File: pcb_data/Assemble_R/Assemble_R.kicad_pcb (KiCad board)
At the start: 2 copper layers, 186.9 x 96.4 mm, 103 parts, among them J1 Conn_01x02, U1 XIAO-nRF52840

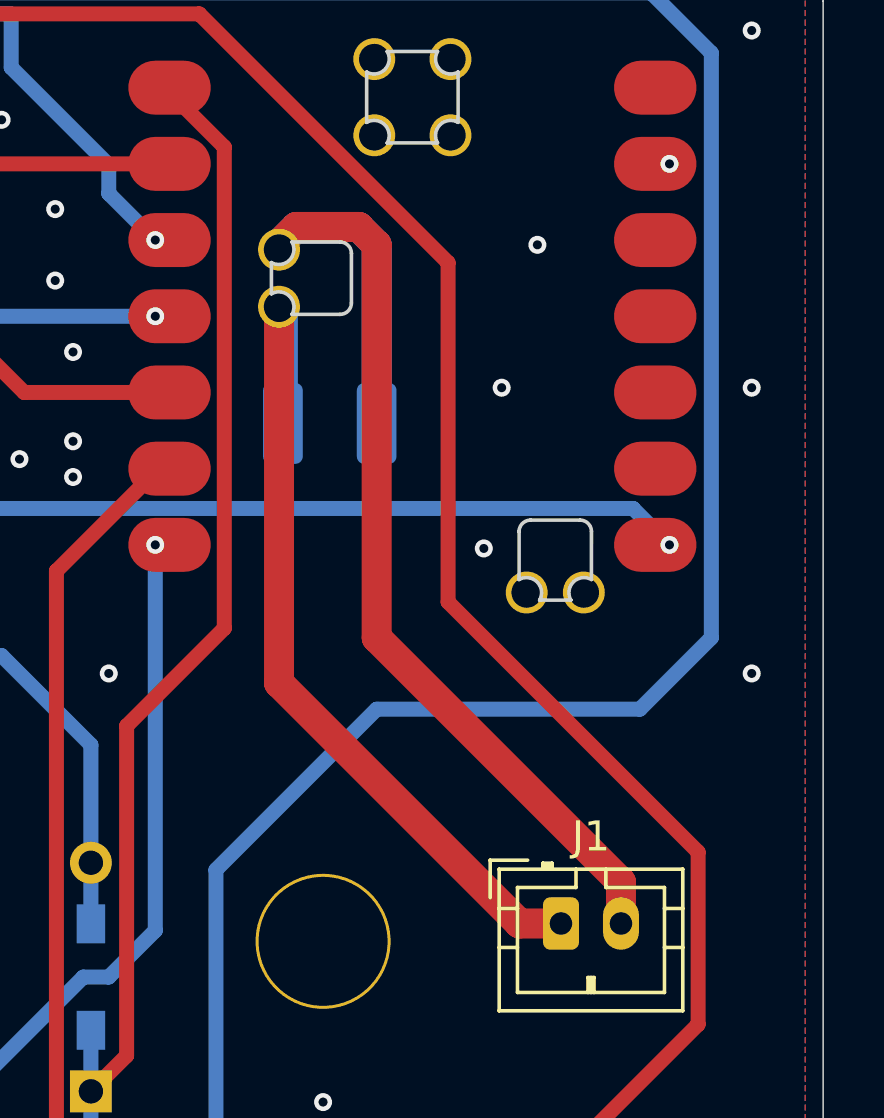
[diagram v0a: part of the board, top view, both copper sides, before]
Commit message: Feat/fix power line width (#24)
* fix power line pattern width

* project file updated
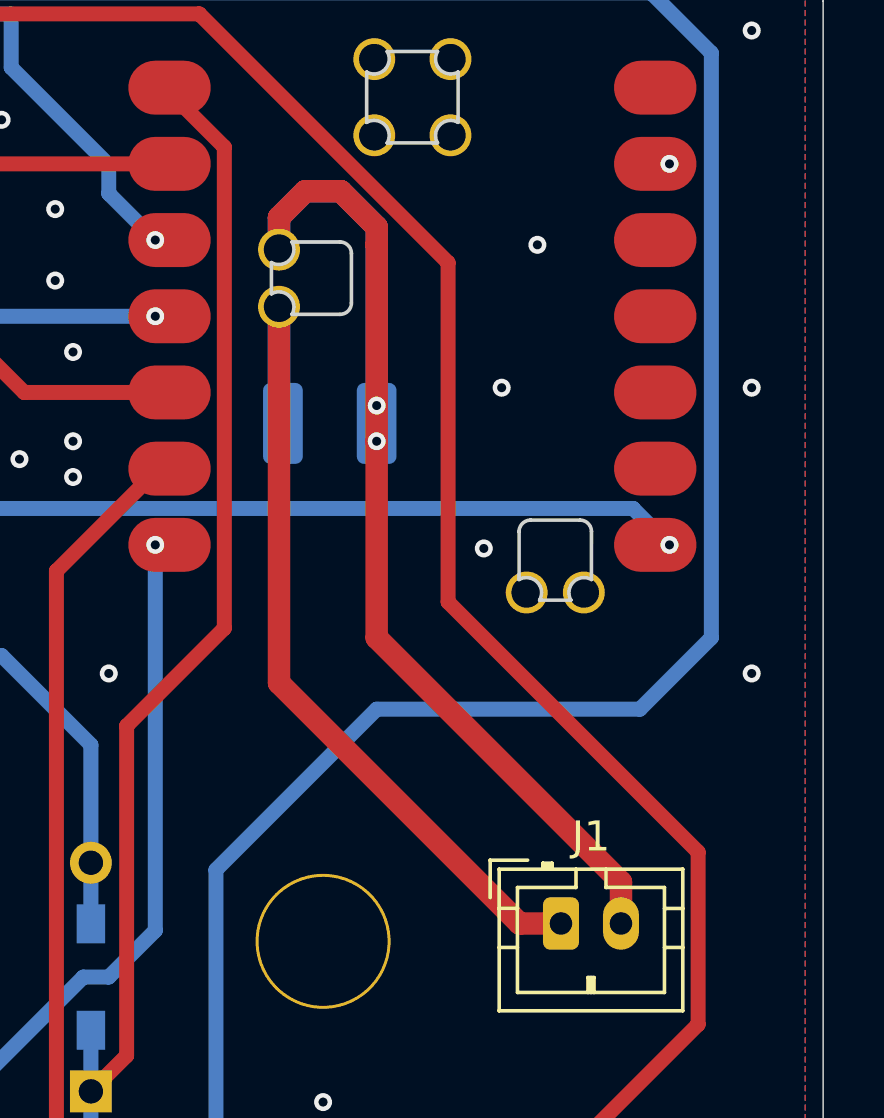
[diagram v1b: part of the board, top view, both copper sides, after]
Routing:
- net GND: track 39.8 -> 43.5 mm, vias 228 -> 230
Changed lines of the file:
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@@
+	)
+	(segment
+		(start 236.339261 55.364109)
+		(end 237.529887 56.554735)
+		(width 0.75)
+		(layer "F.Cu")
+		(net 52)
+	)
+	(segment
+		(start 235.148635 55.364109)
+		(end 236.339261 55.364109)
+		(width 0.75)
+		(layer "F.Cu")
+		(net 52)
+	)
+	(segment
+		(start 237.529887 63.698491)
+		(end 237.529887 57.150048)
+		(width 0.75)
+		(layer "F.Cu")
+		(net 52)
 	)
 	(segment
 		(start 237.529887 70.246934)
 		(end 245.673643 78.39069)
-		(width 1)
+		(width 0.75)
 		(layer "F.Cu")
 		(net 52)
@@
 	(segment
 		(start 237.529887 70.246934)
+		(end 237.529887 63.698491)
+		(width 0.75)
+		(layer "F.Cu")
+		(net 52)
+	)
+	(segment
+		(start 234.275513 56.237231)
+		(end 235.148635 55.364109)
+		(width 0.75)
+		(layer "F.Cu")
+		(net 52)
+	)
+	(segment
+		(start 237.529887 56.554735)
 		(end 237.529887 57.150048)
-		(width 1)
-		(layer "F.Cu")
-		(net 52)
-	)
-	(segment
-		(start 236.934574 56.554735)
-		(end 234.85281 56.554735)
-		(width 1)
-		(layer "F.Cu")
-		(net 52)
-	)
-	(segment
-		(start 234.85281 56.554735)
-		(end 234.275513 57.132032)
-		(width 1)
-		(layer "F.Cu")
-		(net 52)
-	)
-	(segment
-		(start 237.529887 57.150048)
-		(end 236.934574 56.554735)
-		(width 1)
+		(width 0.75)
 		(layer "F.Cu")
 		(net 52)
@@
 		(start 245.673643 78.39069)
 		(end 245.673643 79.771942)
-		(width 1)
-		(layer "F.Cu")
-		(net 52)
-	)
-	(segment
-		(start 234.275513 57.132032)
-		(end 234.275513 57.3092)
-		(width 0.5)
+		(width 0.75)
+		(layer "F.Cu")
+		(net 52)
+	)
+	(segment
+		(start 234.275513 57.3092)
+		(end 234.275513 56.237231)
+		(width 0.75)
 		(layer "F.Cu")
 		(net 52)
@@
 	)
 	(via
+		(at 237.529887 62.507865)
+		(size 0.6)
+		(drill 0.3)
+		(layers "F.Cu" "B.Cu")
+		(net 52)
+	)
+	(via
 		(at 176.2125 61.9125)
 		(size 0.6)
@@
 	)
 	(via
+		(at 237.529887 63.698491)
+		(size 0.6)
+		(drill 0.3)
+		(layers "F.Cu" "B.Cu")
+		(net 52)
+	)
+	(via
 		(at 157.162632 117.871974)
 		(size 0.6)
@@
 	)
 	(segment
-		(start 237.529887 57.150048)
+		(start 236.339261 55.364109)
+		(end 237.529887 56.554735)
+		(width 0.75)
+		(layer "B.Cu")
+		(net 52)
+	)
+	(segment
+		(start 237.529887 56.554735)
+		(end 237.529887 62.507865)
+		(width 0.75)
+		(layer "B.Cu")
+		(net 52)
+	)
+	(segment
+		(start 237.529887 62.507865)
 		(end 237.529887 63.103178)
-		(width 1)
-		(layer "B.Cu")
-		(net 52)
-	)
-	(segment
-		(start 234.85281 56.554735)
-		(end 236.934574 56.554735)
-		(width 1)
-		(layer "B.Cu")
-		(net 52)
-	)
-	(segment
-		(start 236.934574 56.554735)
-		(end 237.529887 57.150048)
-		(width 1)
-		(layer "B.Cu")
-		(net 52)
-	)
-	(segment
-		(start 234.275513 57.132032)
-		(end 234.85281 56.554735)
-		(width 1)
+		(width 0.75)
+		(layer "B.Cu")
+		(net 52)
+	)
+	(segment
+		(start 235.148635 55.364109)
+		(end 236.339261 55.364109)
+		(width 0.75)
 		(layer "B.Cu")
 		(net 52)
@@
 	(segment
 		(start 234.275513 57.3092)
-		(end 234.275513 57.132032)
-		(width 0.5)
+		(end 234.275513 56.237231)
+		(width 0.75)
+		(layer "B.Cu")
+		(net 52)
+	)
+	(segment
+		(start 234.275513 56.237231)
+		(end 235.148635 55.364109)
+		(width 0.75)
 		(layer "B.Cu")
 		(net 52)
@@
 		(start 242.292391 79.771942)
 		(end 243.673643 79.771942)
-		(width 1)
+		(width 0.75)
 		(layer "F.Cu")
 		(net 56)
@@
 		(start 234.275513 71.755064)
 		(end 242.292391 79.771942)
-		(width 1)
+		(width 0.75)
 		(layer "F.Cu")
 		(net 56)
@@
 		(start 234.275513 59.2142)
 		(end 234.275513 71.755064)
-		(width 1)
+		(width 0.75)
 		(layer "F.Cu")
 		(net 56)
 	)
 	(segment
-		(start 234.404887 63.103178)
-		(end 234.404887 59.343574)
-		(width 1)
+		(start 234.275513 62.973804)
+		(end 234.404887 63.103178)
+		(width 0.5)
 		(layer "B.Cu")
 		(net 56)
@@
 		(layer "B.Cu")
 		(net 56)
+	)
+	(segment
+		(start 234.275513 59.2142)
+		(end 234.275513 62.973804)
+		(width 0.75)
+		(layer "B.Cu")
+		(net 56)

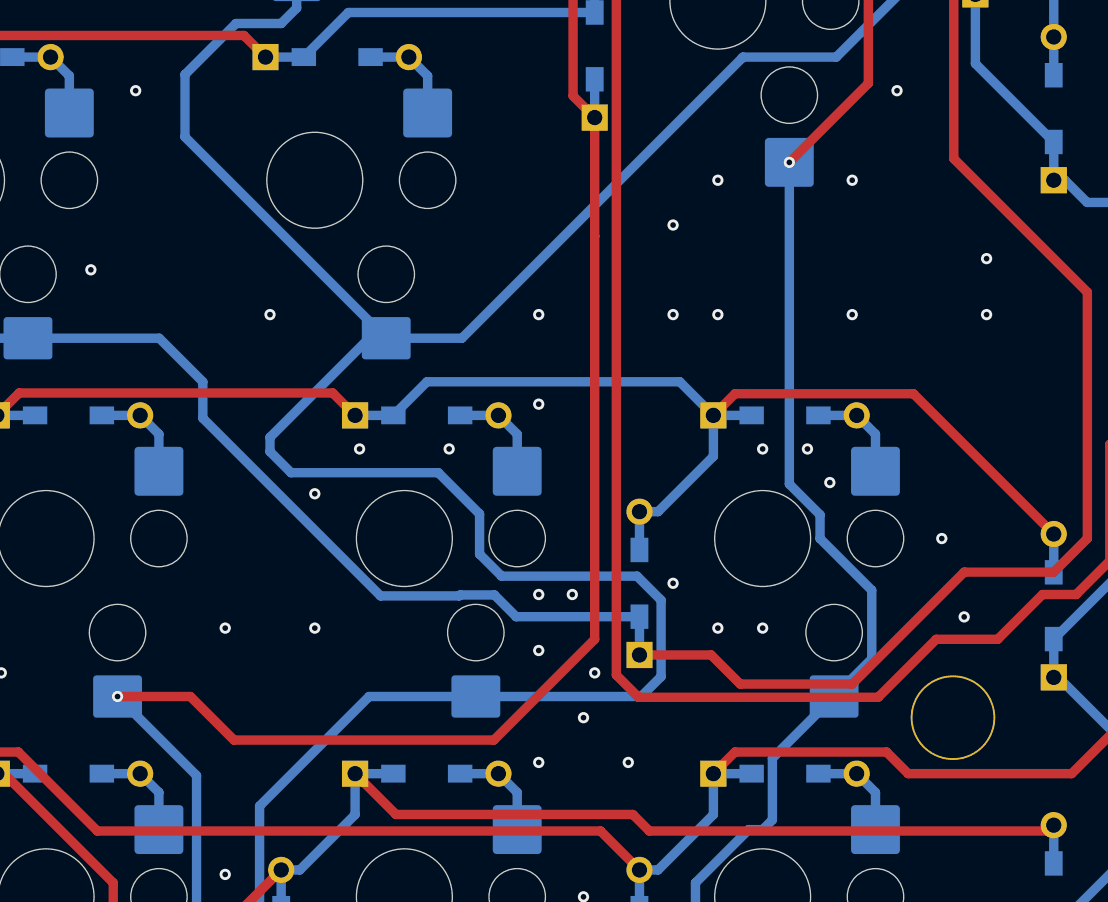
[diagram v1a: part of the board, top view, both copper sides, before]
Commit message: Issue/15 top and bottom plate (#26)
* copy from Assemble

* remove file

* rename file

* remove file

* replace value

* fix position of mounting hole

* copy from Assemble_L

* remove segment and via

* remove zone

* remove diode

* replace switch footprint

* update line

* update footprint

* remove unnecessary footprint

* add step file

* change hole position

* step updated

* add bottom_l project file

* remove unnecessary footprint

* add step file

* copy from Assemble_R

* remove zone, segment and via

* remove diode

* replace switch footprint

* update line

* remove unnecessary footprint

* add step file

* add bottom_r project file

* remove unnecessary footprint

* add step file

* fix hole footprint and number (#25)

* fix line

* Issue/12 build guide (#28)

* add build guide

* update build guide

* Update docs/requirements/requirements_board.md

* Update docs/requirements/requirements_board.md

* Update docs/requirements/requirements_board.md

* Update docs/requirements/requirements_board.md

* Update docs/requirements/requirements_board.md

* Update docs/build_guide.md

* Update docs/build_guide.md

* Update README.md

* Update docs/build_guide.md

* Update docs/build_guide.md

* Update README.md

* Update docs/build_guide.md

* Update docs/build_guide.md

* Update docs/build_guide.md

* Update docs/build_guide.md

* Update docs/build_guide.md

* Update docs/build_guide.md

* Update docs/build_guide.md

* Update docs/build_guide.md

* Update docs/build_guide.md

* Update docs/build_guide.md

* Update docs/build_guide.md

* Update docs/build_guide.md

* Update docs/build_guide.md

* Update docs/build_guide.md

* Update docs/build_guide.md

* Update docs/build_guide.md

* Update docs/build_guide.md

* Update docs/build_guide.md

* Update docs/build_guide.md

* Update docs/build_guide.md

* Update docs/build_guide.md

* Update docs/build_guide.md

* Update docs/build_guide.md

* Update docs/build_guide.md

* Update docs/build_guide.md

* Update doc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
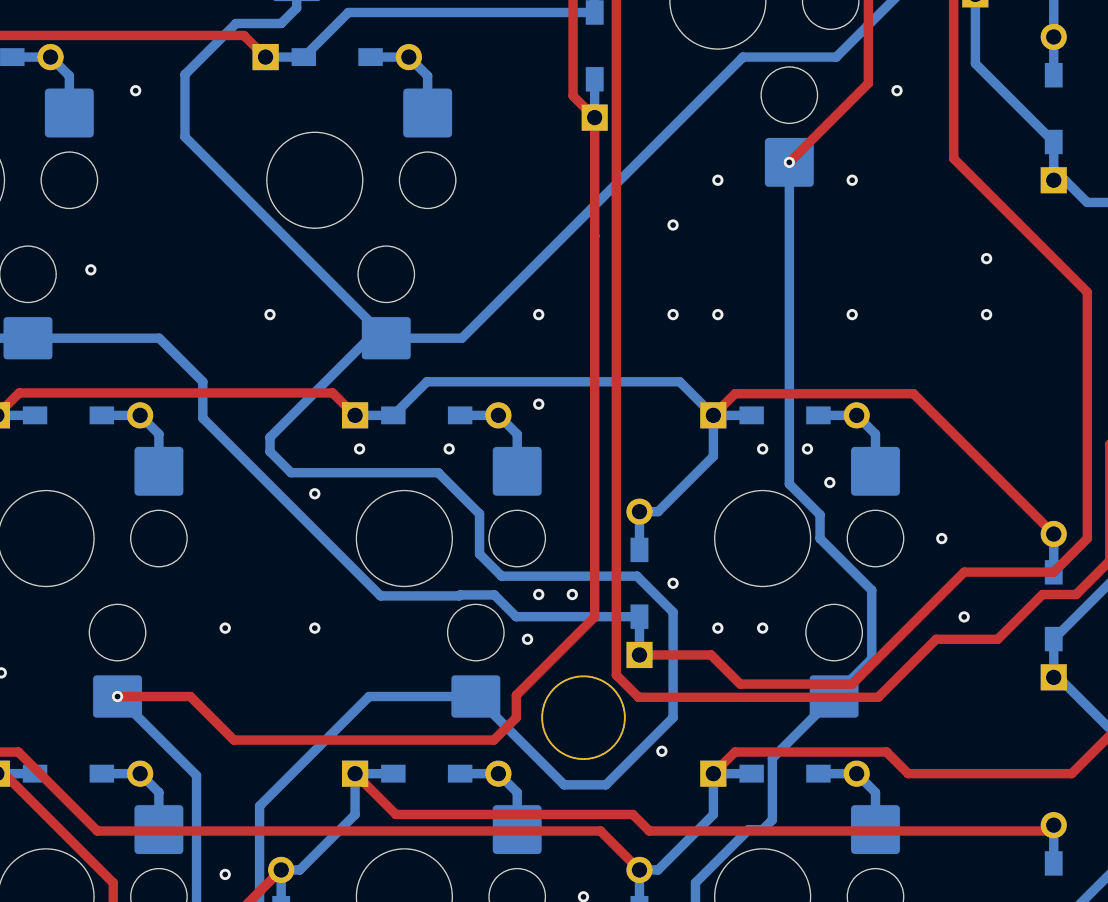
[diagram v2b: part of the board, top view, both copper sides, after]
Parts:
- moved H6 19.6 mm to (207.2, 123.8)
- renumbered H8 to H7, H7 to H8
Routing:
- net IO 12: track 232.4 -> 238.5 mm
- net GND: vias 230 -> 227
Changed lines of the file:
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@@
 	(footprint "kbd_Hole:m2_Spacer_Hole"
 		(layer "F.Cu")
-		(at 226.814253 123.825104)
+		(at 207.168924 123.825104)
 		(descr "Mounting Hole 2.2mm, no annular, M2")
 		(tags "mounting hole 2.2mm no annular m2")
@@
 		(descr "Mounting Hole 2.2mm, no annular, M2")
 		(tags "mounting hole 2.2mm no annular m2")
-		(property "Reference" "H7"
+		(property "Reference" "H8"
 			(at 0 -3.2 0)
 			(layer "F.Fab")
@@
 		(descr "Mounting Hole 2.2mm, no annular, M2")
 		(tags "mounting hole 2.2mm no annular m2")
-		(property "Reference" "H8"
+		(property "Reference" "H7"
 			(at 0 -3.2 0)
 			(layer "F.Fab")
@@
 	)
 	(segment
-		(start 207.764237 98.226719)
-		(end 207.764237 119.657913)
-		(width 0.5)
-		(layer "F.Cu")
-		(net 48)
-	)
-	(segment
-		(start 207.7642 91.9163)
-		(end 207.7642 98.226682)
-		(width 0.5)
-		(layer "F.Cu")
-		(net 48)
-	)
-	(segment
 		(start 220.26581 59.5313)
 		(end 206.6147 73.18241)
@@
 	)
 	(segment
-		(start 182.3938 141.75)
-		(end 139.5313 141.75)
+		(start 188.583177 125.01573)
+		(end 202.40642 125.01573)
 		(width 0.5)
 		(layer "F.Cu")
@@
 	)
 	(segment
-		(start 207.764237 119.657913)
-		(end 202.40642 125.01573)
+		(start 182.3938 141.75)
+		(end 139.5313 141.75)
 		(width 0.5)
 		(layer "F.Cu")
@@
 	)
 	(segment
+		(start 207.764237 118.467287)
+		(end 207.764237 98.226719)
+		(width 0.5)
+		(layer "F.Cu")
+		(net 48)
+	)
+	(segment
+		(start 207.764237 98.226719)
+		(end 207.7642 98.226682)
+		(width 0.5)
+		(layer "F.Cu")
+		(net 48)
+	)
+	(segment
 		(start 225.782275 62.0712)
 		(end 223.242375 59.5313)
@@
 	)
 	(segment
-		(start 202.40642 125.01573)
+		(start 186.267447 122.7)
 		(end 188.583177 125.01573)
 		(width 0.5)
@@
 	)
 	(segment
-		(start 188.583177 125.01573)
+		(start 182.3938 122.7)
 		(end 186.267447 122.7)
 		(width 0.5)
@@
 	)
 	(segment
-		(start 186.267447 122.7)
-		(end 182.3938 122.7)
+		(start 202.40642 125.01573)
+		(end 203.597046 123.825104)
+		(width 0.5)
+		(layer "F.Cu")
+		(net 48)
+	)
+	(segment
+		(start 203.597046 122.634478)
+		(end 207.764237 118.467287)
 		(width 0.5)
 		(layer "F.Cu")
@@
 	(segment
 		(start 207.7642 98.226682)
-		(end 207.764237 98.226719)
+		(end 207.7642 91.9163)
+		(width 0.5)
+		(layer "F.Cu")
+		(net 48)
+	)
+	(segment
+		(start 203.597046 123.825104)
+		(end 203.597046 122.634478)
 		(width 0.5)
 		(layer "F.Cu")
@@
 	)
 	(segment
-		(start 191.622065 110.801)
-		(end 199.45093 110.801)
-		(width 0.5)
-		(layer "B.Cu")
-		(net 50)
-	)
-	(segment
 		(start 196.6813 103.65)
 		(end 185.9803 92.949)
@@
 	)
 	(segment
-		(start 201.6428 115.128841)
-		(end 202.814959 116.301)
-		(width 0.5)
-		(layer "B.Cu")
-		(net 50)
-	)
-	(segment
 		(start 200.702266 103.65)
 		(end 196.6813 103.65)
@@
 	)
 	(segment
-		(start 190.50016 109.679095)
-		(end 191.622065 110.801)
-		(width 0.5)
-		(layer "B.Cu")
-		(net 50)
-	)
-	(segment
 		(start 228.600192 81.557881)
 		(end 227.752879 81.557881)
@@
 	)
 	(segment
+		(start 206.140782 127.396982)
+		(end 201.4438 122.7)
+		(width 0.5)
+		(layer "B.Cu")
+		(net 50)
+	)
+	(segment
+		(start 211.931428 118.215228)
+		(end 211.931428 123.825104)
+		(width 0.5)
+		(layer "B.Cu")
+		(net 50)
+	)
+	(segment
 		(start 215.576968 88.775299)
 		(end 200.702266 103.65)
@@
 	)
 	(segment
-		(start 190.50016 108.920905)
-		(end 190.50016 109.679095)
+		(start 201.6428 112.99287)
+		(end 201.6428 115.128841)
 		(width 0.5)
 		(layer "B.Cu")
@@
 	)
 	(segment
+		(start 196.6813 103.65)
+		(end 195.771065 103.65)
+		(width 0.5)
+		(layer "B.Cu")
+		(net 50)
+	)
+	(segment
 		(start 191.9188 84.6)
 		(end 191.9188 86.092371)
@@
 	)
 	(segment
-		(start 210.2358 122.7)
-		(end 201.4438 122.7)
-		(width 0.5)
-		(layer "B.Cu")
-		(net 50)
-	)
-	(segment
-		(start 211.295 121.6408)
-		(end 210.2358 122.7)
+		(start 201.6428 115.128841)
+		(end 202.814959 116.301)
 		(width 0.5)
 		(layer "B.Cu")
@@
 	)
 	(segment
-		(start 196.6813 103.65)
-		(end 195.771065 103.65)
+		(start 211.931428 123.825104)
+		(end 208.35955 127.396982)
 		(width 0.5)
 		(layer "B.Cu")
@@
 	)
 	(segment
+		(start 191.622065 110.801)
+		(end 199.45093 110.801)
+		(width 0.5)
+		(layer "B.Cu")
+		(net 50)
+	)
+	(segment
+		(start 202.814959 116.301)
+		(end 210.0172 116.301)
+		(width 0.5)
+		(layer "B.Cu")
+		(net 50)
+	)
+	(segment
 		(start 201.4438 122.7)
 		(end 195.771065 122.7)
@@
 	)
 	(segment
-		(start 201.6428 112.99287)
-		(end 201.6428 115.128841)
+		(start 199.45093 110.801)
+		(end 201.6428 112.99287)
 		(width 0.5)
 		(layer "B.Cu")
@@
 	)
 	(segment
-		(start 211.295 117.5788)
-		(end 211.295 121.6408)
-		(width 0.5)
-		(layer "B.Cu")
-		(net 50)
-	)
-	(segment
 		(start 230.150553 67.1512)
 		(end 230.150553 80.00752)
@@
 	)
 	(segment
-		(start 199.45093 110.801)
-		(end 201.6428 112.99287)
-		(width 0.5)
-		(layer "B.Cu")
-		(net 50)
-	)
-	(segment
 		(start 189.946 140.6909)
 		(end 191.0051 141.75)
@@
 	)
 	(segment
-		(start 210.0172 116.301)
-		(end 211.295 117.5788)
-		(width 0.5)
-		(layer "B.Cu")
-		(net 50)
-	)
-	(segment
 		(start 195.771065 103.65)
 		(end 190.50016 108.920905)
@@
 	)
 	(segment
-		(start 202.814959 116.301)
-		(end 210.0172 116.301)
+		(start 190.50016 109.679095)
+		(end 191.622065 110.801)
 		(width 0.5)
 		(layer "B.Cu")
@@
 	)
 	(segment
+		(start 210.0172 116.301)
+		(end 211.931428 118.215228)
+		(width 0.5)
+		(layer "B.Cu")
+		(net 50)
+	)
+	(segment
 		(start 191.9188 84.6)
 		(end 172.8688 84.6)
@@
 	)
 	(segment
+		(start 190.50016 108.920905)
+		(end 190.50016 109.679095)
+		(width 0.5)
+		(layer "B.Cu")
+		(net 50)
+	)
+	(segment
+		(start 208.35955 127.396982)
+		(end 206.140782 127.396982)
+		(width 0.5)
+		(layer "B.Cu")
+		(net 50)
+	)
+	(segment
 		(start 218.1125 94.3)
 		(end 222.3135 90.099)
@@
 	)
 	(via
-		(at 207.16875 123.825)
-		(size 0.6)
-		(drill 0.3)
-		(layers "F.Cu" "B.Cu")
-		(free yes)
-		(net 52)
-	)
-	(via
 		(at 69.05625 126.20625)
 		(size 0.6)
@@
 	)
 	(via
-		(at 207.764237 121.443852)
-		(size 0.6)
-		(drill 0.3)
-		(layers "F.Cu" "B.Cu")
-		(free yes)
-		(net 52)
-	)
-	(via
 		(at 240.50625 135.73125)
 		(size 0.6)
@@
 	)
 	(via
+		(at 204.192359 119.657913)
+		(size 0.6)
+		(drill 0.3)
+		(layers "F.Cu" "B.Cu")
+		(free yes)
+		(net 52)
+	)
+	(via
 		(at 204.7875 140.49375)
 		(size 0.6)
@@
 	)
 	(via
-		(at 204.7875 126.20625)
+		(at 211.336115 125.611043)
 		(size 0.6)
 		(drill 0.3)
@@
 	)
 	(via
-		(at 204.787672 120.253226)
-		(size 0.6)
-		(drill 0.3)
-		(layers "F.Cu" "B.Cu")
-		(free yes)
-		(net 52)
-	)
-	(via
 		(at 227.409566 118.467287)
 		(size 0.6)
@@
 		(size 0.6)
 		(drill 0.3)
-		(layers "F.Cu" "B.Cu")
-		(free yes)
-		(net 52)
-	)
-	(via
-		(at 209.55 126.20625)
-		(size 0.6)
-		(drill 0.3)
